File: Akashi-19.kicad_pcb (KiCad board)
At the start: 2 copper layers, 111.8 x 96.5 mm, 7 parts, among them J1 Conn_01x20_Socket, J2 Conn_01x20_Socket, J3 GROVE I2C, J4 QWIIC, J5 SERIAL, SW1 RESET, U1 Raspberry Pi Pico

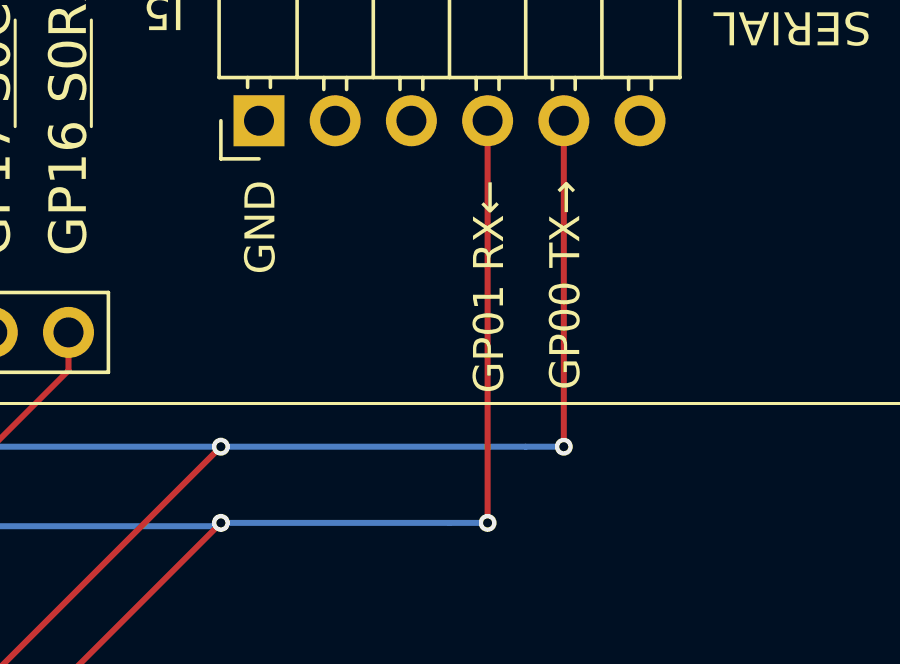
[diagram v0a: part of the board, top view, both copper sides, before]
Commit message: Add "N.C." explicitly to the pin description of serial port.
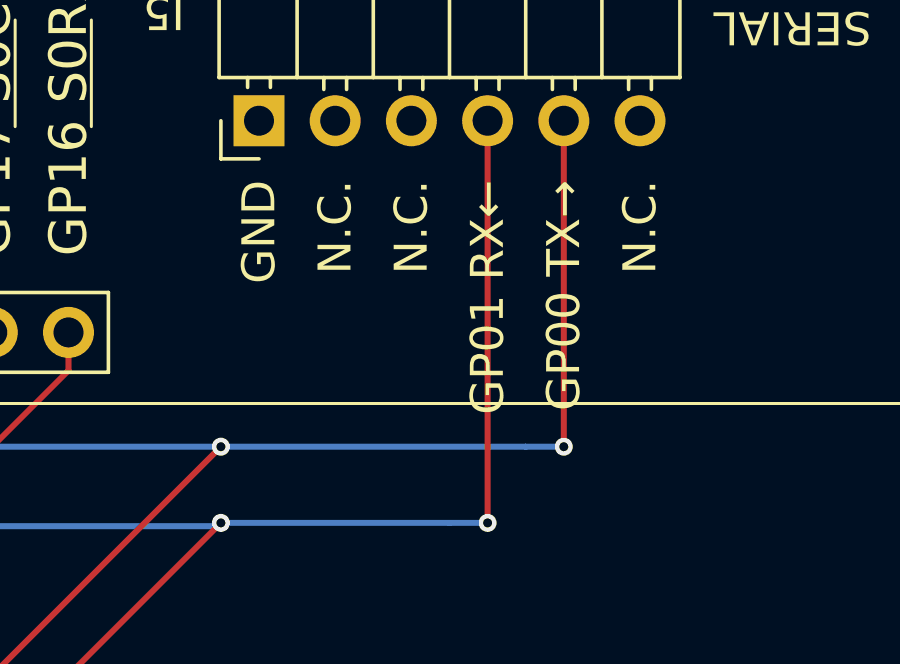
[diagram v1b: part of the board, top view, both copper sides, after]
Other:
- board text added: "N.C."

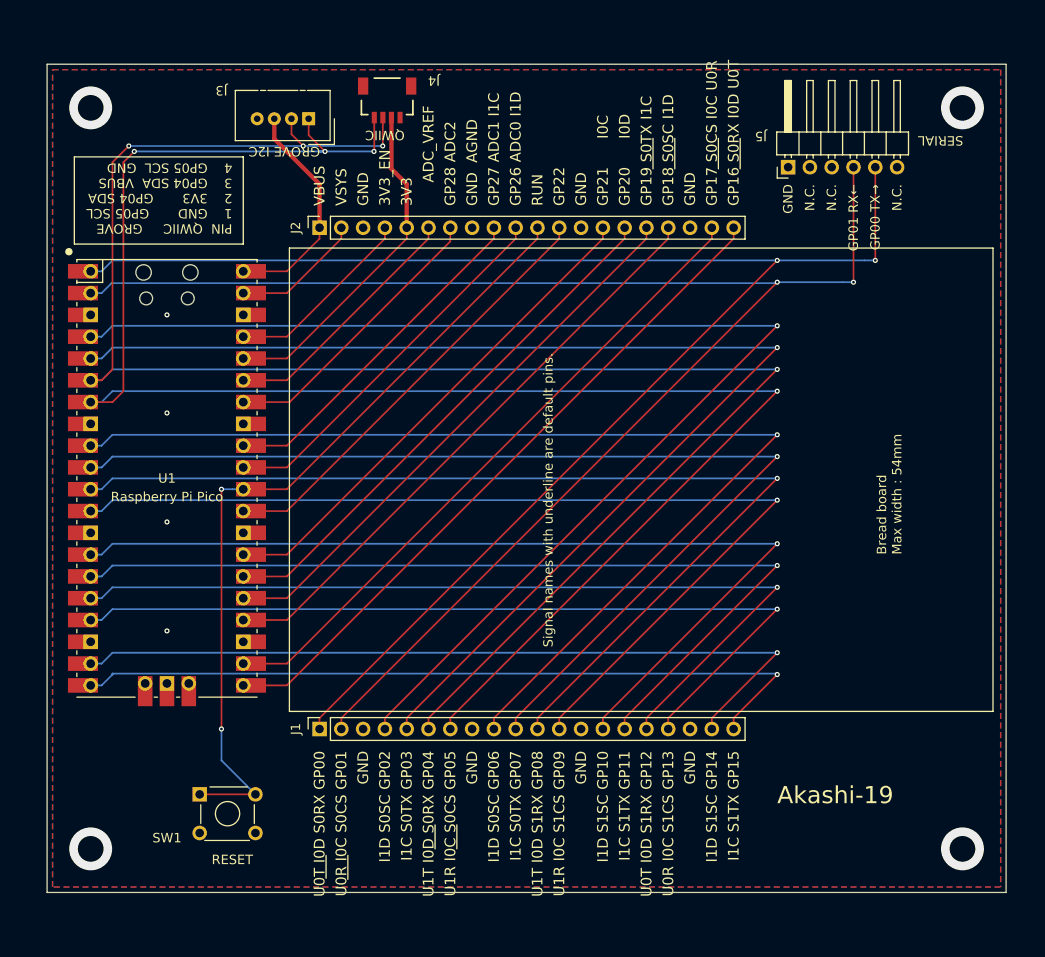
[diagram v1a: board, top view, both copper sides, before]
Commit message: Expand board size by 2.54mm.
To give the margin to the breadboad.
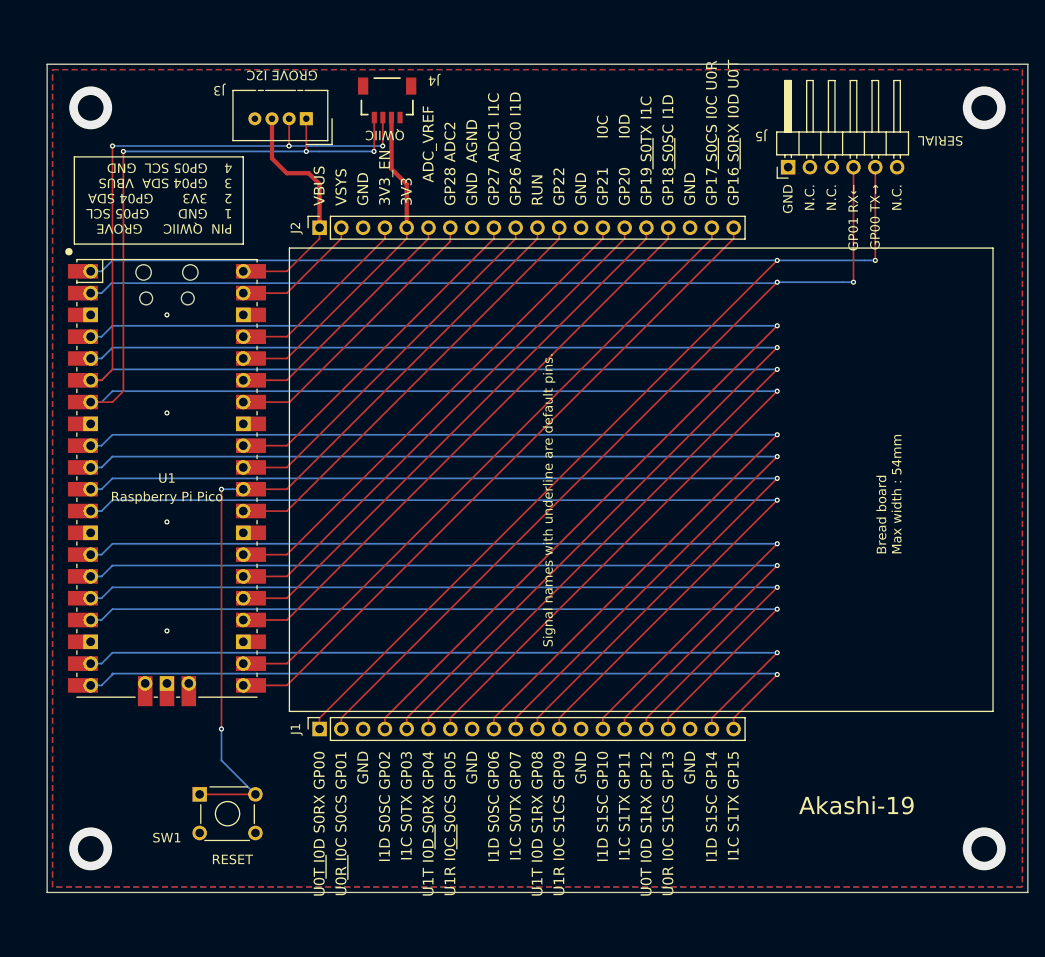
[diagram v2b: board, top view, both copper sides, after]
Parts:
- moved J3 0.27 mm to (128.0, 58.4)
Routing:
- net +5V: track 26.6 -> 28.4 mm
- net /SCL: track 206.3 -> 205.0 mm
- net /SDA: track 205.8 -> 206.4 mm
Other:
- board size 111.8 x 96.5 mm -> 114.3 x 96.5 mm

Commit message: Adjust the postion of SW and serial port.
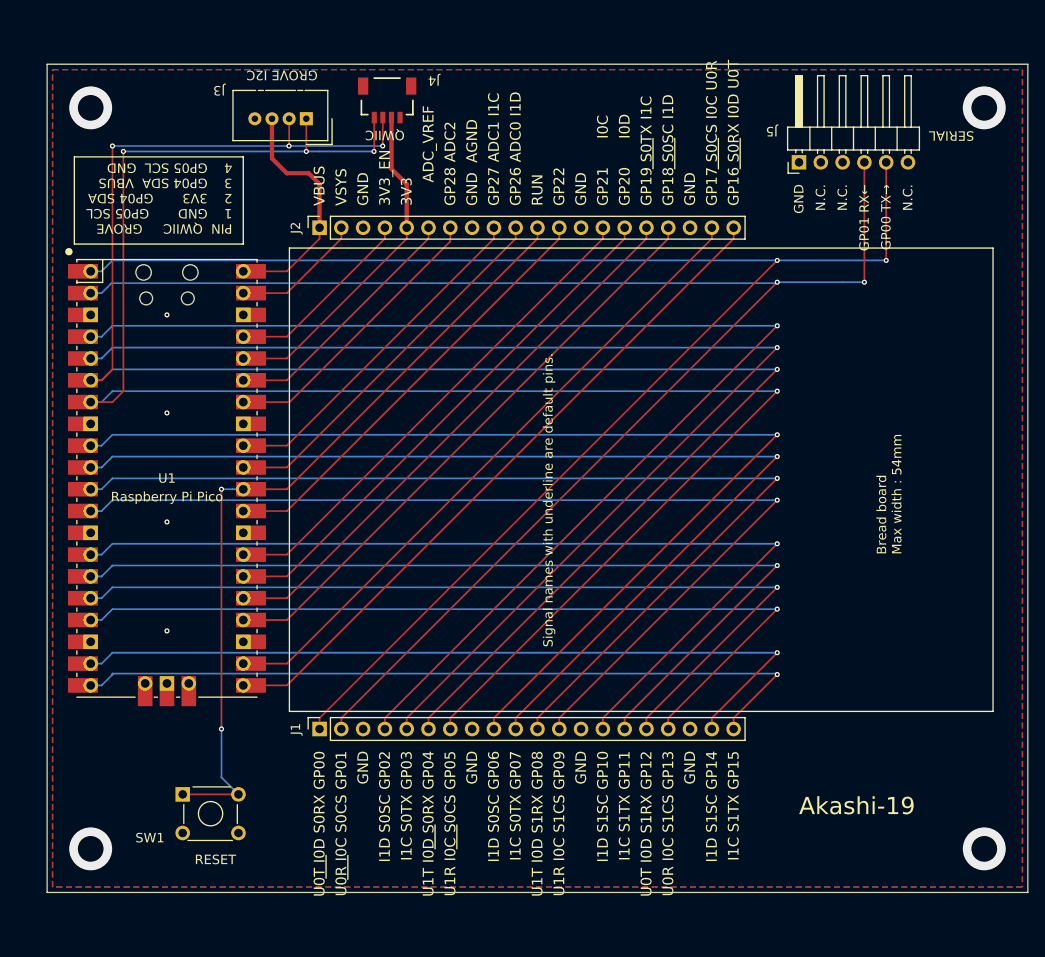
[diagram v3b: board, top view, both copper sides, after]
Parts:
- moved SW1 1.98 mm to (113.6, 137.2)
- moved J5 1.39 mm to (185.4, 63.5)
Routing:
- net /TX: track 179.5 -> 180.8 mm
- net /RX: track 175.9 -> 177.2 mm
- net Net-(J2-Pin_11): track 93.9 -> 93.1 mm
